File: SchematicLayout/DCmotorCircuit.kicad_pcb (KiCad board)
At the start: 2 copper layers, 68.6 x 53.3 mm, 12 parts, among them J1 Power, J2 Digital/PWM, J3 Analog, J4 Digital/PWM, J5 MotorConnector, J6 Conn_01x01_Socket, SW1 RotaryEncoder_Switch, U1 DRV8833

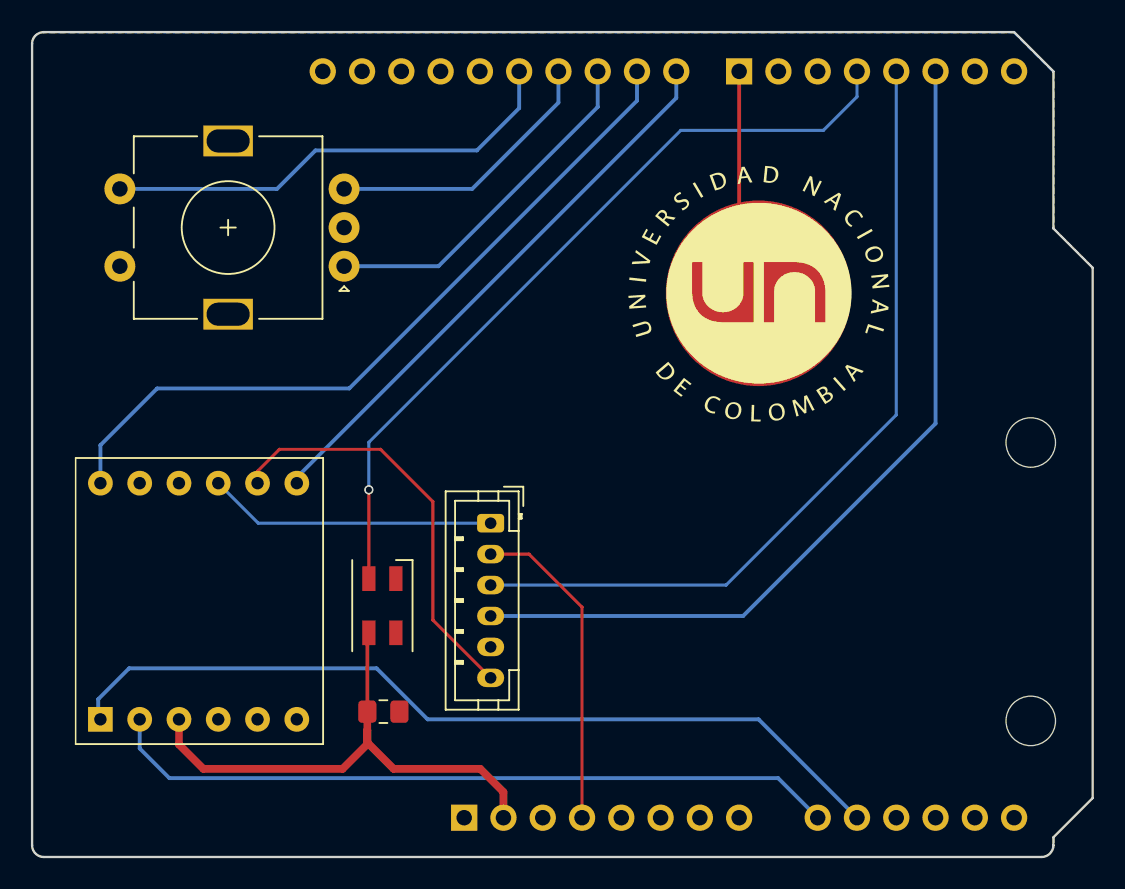
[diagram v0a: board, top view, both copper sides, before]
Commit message: circuit updated with analog filter for the encoder GY-40
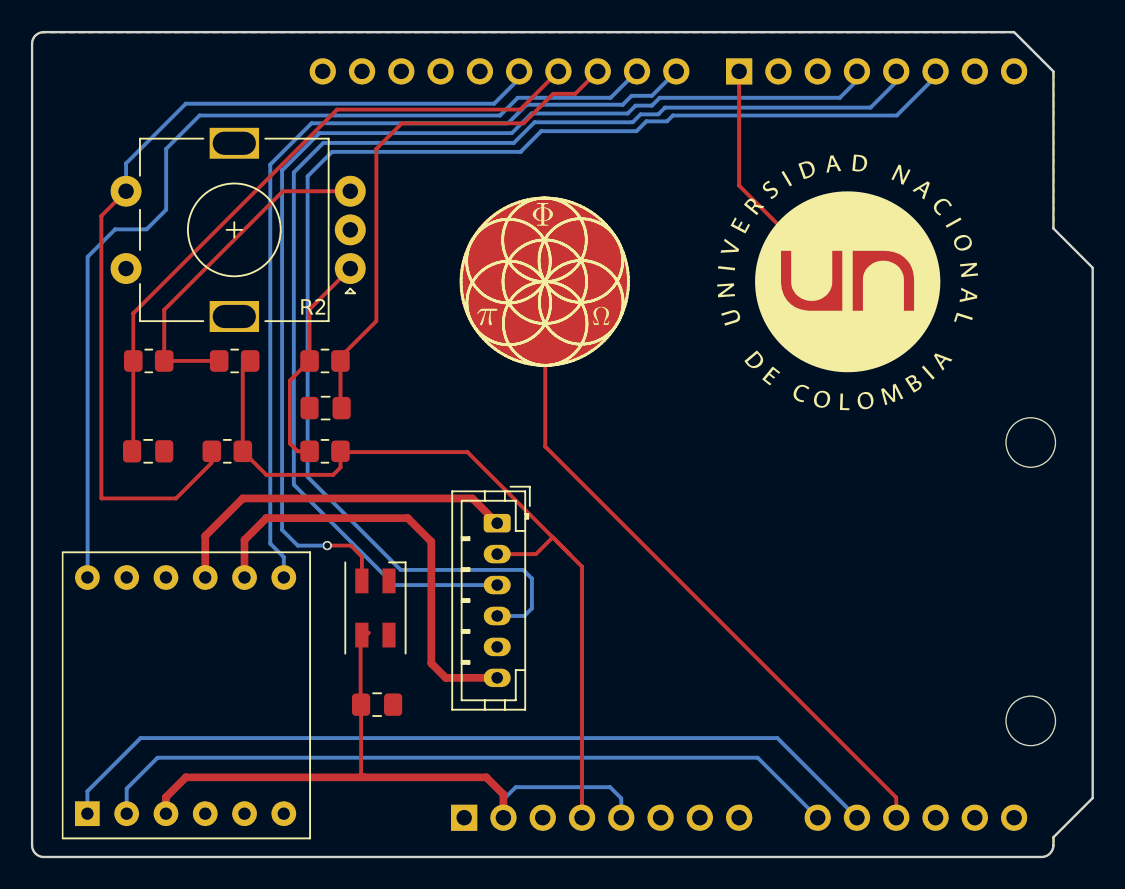
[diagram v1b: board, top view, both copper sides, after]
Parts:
- removed J6: Conn_01x01_Socket, Connector_PinHeader_1.00mm:PinHeader_1x01_P1.00mm_Vertical
- added C2: 100nF, Capacitor_SMD:C_0805_2012Metric_Pad1.18x1.45mm_HandSolder, F.Cu at (135.4, 96.8)
- added C3: 100nF, Capacitor_SMD:C_0805_2012Metric_Pad1.18x1.45mm_HandSolder, F.Cu at (123.9, 99.6)
- added P1: UN, MountingHole:MountingHole_5mm_Pad_TopOnly, F.Cu at (169.2, 88.6)
- added P2: LF, MountingHole:MountingHole_5mm_Pad_TopOnly, F.Cu at (149.6, 88.6)
- added R1: 10k, Resistor_SMD:R_0805_2012Metric_Pad1.20x1.40mm_HandSolder, F.Cu at (135.4, 99.6)
- added R2: 10k, Resistor_SMD:R_0805_2012Metric_Pad1.20x1.40mm_HandSolder, F.Cu at (135.4, 93.7)
- added R3: 10k, Resistor_SMD:R_0805_2012Metric_Pad1.20x1.40mm_HandSolder, F.Cu at (129.5, 93.7)
- added R4: 10k, Resistor_SMD:R_0805_2012Metric_Pad1.20x1.40mm_HandSolder, F.Cu at (124.0, 93.7)
- added R5: 10k, Resistor_SMD:R_0805_2012Metric_Pad1.20x1.40mm_HandSolder, F.Cu at (129.0, 99.6)
- C1: value C -> 100nF
- moved U1 6.16 mm to (120.0, 123.0)
- moved C1 0.60 mm to (138.7, 116.0)
- moved D1 0.47 mm to (138.6, 109.7)
- moved SW1 0.43 mm to (137.0, 87.8)
- moved J5 0.42 mm to (146.5, 104.2)
- renumbered REF** to REF1, REF** to REF2
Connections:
- SW1 pad A: /IO10 -> Net-(R1-Pad2)
- SW1 pad B: /IO11 -> Net-(R3-Pad2)
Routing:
- net /IO7: track 0.00 -> 43.1 mm
- net +3V3: track 20.9 -> 54.5 mm
- net /IO18: track 57.2 -> 86.3 mm
- net /IO13: track 30.4 -> 58.6 mm
- net /IO17: track 53.0 -> 78.1 mm
- net /IO11: track 18.2 -> 42.7 mm
- net Net-(R3-Pad2): track 0.00 -> 21.8 mm
- net /IO19: track 51.3 -> 70.9 mm
- net /IO21: track 36.6 -> 55.8 mm
- net /IO46: track 48.0 -> 63.9 mm
- net Net-(R1-Pad2): track 0.00 -> 14.2 mm
- net +5V: track 35.1 -> 46.5 mm
- net /IO10: track 23.0 -> 33.9 mm
- net /M2_R: track 19.0 -> 23.2 mm
- net /IO14: track 14.5 -> 17.3 mm
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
